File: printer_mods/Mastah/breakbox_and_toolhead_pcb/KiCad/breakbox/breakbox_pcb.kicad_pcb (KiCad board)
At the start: 2 copper layers, 60 x 50 mm, 18 parts

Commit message: Update PCBs and fix some issues
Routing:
- net (no net): track 621.3 -> 626.9 mm
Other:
- board text added: "V1.1 Breakbox Design by Mastah"
- board text removed: "V1.0 Breakbox Design by Mastah"
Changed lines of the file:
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@@
     (effects (font (size 0.6 0.6) (thickness 0.1)))
   )
-  (gr_text "V1.0\n\nBreakbox\n\nDesign by\nMastah" (at 87.3 79) (layer "F.SilkS")
+  (gr_text "V1.1\n\nBreakbox\n\nDesign by\nMastah" (at 87.3 79) (layer "F.SilkS")
     (effects (font (size 0.6 0.6) (thickness 0.1)) (justify left))
   )
@@
     (effects (font (size 0.6 0.6) (thickness 0.1)))
   )
-  (gr_text "Fan0\nVCC" (at 70.7 76.2) (layer "F.SilkS")
+  (gr_text "Fan0\nVCC" (at 73.5 76.2) (layer "F.SilkS")
     (effects (font (size 0.6 0.6) (thickness 0.1)))
   )
@@
     (effects (font (size 0.6 0.6) (thickness 0.1)))
   )
-  (gr_text "Fan0\nGND" (at 73.5 76.2) (layer "F.SilkS")
+  (gr_text "Fan0\nGND" (at 70.8 76.2) (layer "F.SilkS")
     (effects (font (size 0.6 0.6) (thickness 0.1)))
   )
@@
     (effects (font (size 0.6 0.6) (thickness 0.1)))
   )
-  (gr_text "Fan1\nGND" (at 82.3 76.2) (layer "F.SilkS")
+  (gr_text "Fan1\nGND" (at 79.5 76.2) (layer "F.SilkS")
     (effects (font (size 0.6 0.6) (thickness 0.1)))
   )
@@
     (effects (font (size 0.6 0.6) (thickness 0.1)))
   )
-  (gr_text "Fan1\nVCC" (at 79.6 76.2) (layer "F.SilkS")
+  (gr_text "Fan1\nVCC" (at 82.3 76.2) (layer "F.SilkS")
     (effects (font (size 0.6 0.6) (thickness 0.1)))
   )
@@
   (segment (start 73.3 83.125) (end 73.3 81.525) (width 0.508) (layer "F.Cu") (net 0))
   (segment (start 90 63) (end 97 63) (width 1.524) (layer "F.Cu") (net 0))
-  (segment (start 70.85 72.3) (end 70.85 70.85) (width 0.762) (layer "F.Cu") (net 0))
   (segment (start 76.6 58) (end 99.4 58) (width 0.762) (layer "F.Cu") (net 0))
   (segment (start 78.37 59.97) (end 83.4 65) (width 0.508) (layer "F.Cu") (net 0))
+  (segment (start 73.35 72.3) (end 73.35 70.65) (width 0.762) (layer "F.Cu") (net 0))
   (segment (start 87.2 95.8) (end 92.7 95.8) (width 0.762) (layer "F.Cu") (net 0))
   (segment (start 88.5 59.97) (end 88.5 61.5) (width 1.524) (layer "F.Cu") (net 0))
   (segment (start 59.3 73.9) (end 60.7 75.3) (width 0.508) (layer "F.Cu") (net 0))
-  (segment (start 79.65 72.3) (end 79.65 70.45) (width 0.762) (layer "F.Cu") (net 0))
   (segment (start 81.4 93.8) (end 81.4 92.5) (width 0.762) (layer "F.Cu") (net 0))
   (segment (start 92.7 85.4) (end 94.1 84) (width 0.762) (layer "F.Cu") (net 0))
+  (segment (start 73.35 70.65) (end 75 69) (width 0.762) (layer "F.Cu") (net 0))
   (segment (start 62.7 59.1) (end 63.8 58) (width 0.762) (layer "F.Cu") (net 0))
-  (segment (start 72.7 69) (end 81.8 69) (width 0.762) (layer "F.Cu") (net 0))
   (segment (start 68.2 90.95) (end 70.55 88.6) (width 0.508) (layer "F.Cu") (net 0))
   (segment (start 95.1 87) (end 97 87) (width 0.762) (layer "F.Cu") (net 0))
+  (segment (start 83.7 69) (end 88.3 69) (width 0.762) (layer "F.Cu") (net 0))
   (segment (start 97 68.6) (end 97 69) (width 0.508) (layer "F.Cu") (net 0))
   (segment (start 83.4 65) (end 96 65) (width 0.508) (layer "F.Cu") (net 0))
@@
   (segment (start 86.4 93.8) (end 86.4 95) (width 0.762) (layer "F.Cu") (net 0))
   (segment (start 92.7 95.8) (end 100 88.5) (width 0.762) (layer "F.Cu") (net 0))
-  (segment (start 81.8 69) (end 94 69) (width 0.762) (layer "F.Cu") (net 0))
   (segment (start 94.1 84) (end 97 84) (width 0.762) (layer "F.Cu") (net 0))
   (segment (start 98.5 73.5) (end 100 75) (width 0.508) (layer "F.Cu") (net 0))
@@
   (segment (start 93.5 82.5) (end 98.5 82.5) (width 0.508) (layer "F.Cu") (net 0))
   (segment (start 83.6 90.3) (end 90.8 90.3) (width 0.762) (layer "F.Cu") (net 0))
-  (segment (start 79.65 70.45) (end 81.1 69) (width 0.762) (layer "F.Cu") (net 0))
-  (segment (start 70.85 70.85) (end 72.7 69) (width 0.762) (layer "F.Cu") (net 0))
   (segment (start 87.4 88.6) (end 93.5 82.5) (width 0.508) (layer "F.Cu") (net 0))
-  (segment (start 94 69) (end 97 72) (width 0.762) (layer "F.Cu") (net 0))
   (segment (start 83.9 92.2) (end 84.4 91.7) (width 0.762) (layer "F.Cu") (net 0))
   (segment (start 63.8 58) (end 76.6 58) (width 0.762) (layer "F.Cu") (net 0))
@@
   (segment (start 92.9 81) (end 97 81) (width 0.508) (layer "F.Cu") (net 0))
   (segment (start 56.8 74.1) (end 59.1 76.4) (width 0.508) (layer "F.Cu") (net 0))
+  (segment (start 82.15 70.55) (end 83.7 69) (width 0.762) (layer "F.Cu") (net 0))
+  (segment (start 82.15 72.3) (end 82.15 70.55) (width 0.762) (layer "F.Cu") (net 0))
   (segment (start 69.8 62.2) (end 78.4 62.2) (width 0.508) (layer "F.Cu") (net 0))
   (segment (start 71.15 79.8) (end 80.9 79.8) (width 0.508) (layer "F.Cu") (net 0))
@@
   (segment (start 94.2 88.9) (end 94.2 87.9) (width 0.762) (layer "F.Cu") (net 0))
   (segment (start 58.1 79.8) (end 55.5 82.4) (width 0.508) (layer "F.Cu") (net 0))
-  (segment (start 81.1 69) (end 81.8 69) (width 0.762) (layer "F.Cu") (net 0))
   (segment (start 68.2 93.8) (end 68.2 90.95) (width 0.508) (layer "F.Cu") (net 0))
   (segment (start 65.7 93.8) (end 65.7 90.9) (width 0.508) (layer "F.Cu") (net 0))
   (segment (start 82.1 81) (end 82.1 83.15) (width 0.508) (layer "F.Cu") (net 0))
+  (segment (start 94 69) (end 97 72) (width 0.762) (layer "F.Cu") (net 0))
+  (segment (start 75 69) (end 94 69) (width 0.762) (layer "F.Cu") (net 0))
   (segment (start 70.8 83.125) (end 70.8 81.7) (width 0.508) (layer "F.Cu") (net 0))
   (segment (start 58 82.2) (end 58 83.225) (width 0.508) (layer "F.Cu") (net 0))
@@
   (segment (start 75.4 58) (end 76.6 58) (width 0.508) (layer "F.Cu") (net 0))
   (segment (start 95.4 79.5) (end 98.5 79.5) (width 0.508) (layer "B.Cu") (net 0))
-  (segment (start 82.15 72.7) (end 82.15 71.35) (width 0.508) (layer "B.Cu") (net 0))
   (segment (start 97.5 93.8) (end 102 89.3) (width 0.762) (layer "B.Cu") (net 0))
+  (segment (start 80.3 70.5) (end 98.5 70.5) (width 0.508) (layer "B.Cu") (net 0))
   (segment (start 98.5 79.5) (end 100 78) (width 0.508) (layer "B.Cu") (net 0))
   (segment (start 62.5 74.5) (end 91.2 74.5) (width 0.508) (layer "B.Cu") (net 0))
+  (segment (start 70.85 72.3) (end 70.85 70.75) (width 0.508) (layer "B.Cu") (net 0))
   (segment (start 94.2 60.4) (end 98.4 60.4) (width 1.524) (layer "B.Cu") (net 0))
-  (segment (start 82.15 71.35) (end 83 70.5) (width 0.508) (layer "B.Cu") (net 0))
+  (segment (start 98.5 70.5) (end 100 72) (width 0.508) (layer "B.Cu") (net 0))
   (segment (start 61.8 73.8) (end 62.5 74.5) (width 0.508) (layer "B.Cu") (net 0))
   (segment (start 85.5 59.97) (end 85.5 61.3) (width 1.524) (layer "B.Cu") (net 0))
-  (segment (start 98.5 67.5) (end 100 69) (width 0.508) (layer "B.Cu") (net 0))
   (segment (start 102 89.3) (end 102 86) (width 0.762) (layer "B.Cu") (net 0))
   (segment (start 87 87.9) (end 95.4 79.5) (width 0.508) (layer "B.Cu") (net 0))
   (segment (start 102 86) (end 100 84) (width 0.762) (layer "B.Cu") (net 0))
+  (segment (start 74.1 67.5) (end 98.5 67.5) (width 0.508) (layer "B.Cu") (net 0))
   (segment (start 73.8 87.9) (end 87 87.9) (width 0.508) (layer "B.Cu") (net 0))
-  (segment (start 73.35 70.35) (end 76.2 67.5) (width 0.508) (layer "B.Cu") (net 0))
+  (segment (start 98.5 67.5) (end 100 69) (width 0.508) (layer "B.Cu") (net 0))
   (segment (start 87.2 63) (end 91.6 63) (width 1.524) (layer "B.Cu") (net 0))
   (segment (start 98.4 60.4) (end 100 62) (width 1.524) (layer "B.Cu") (net 0))
-  (segment (start 98.5 70.5) (end 100 72) (width 0.508) (layer "B.Cu") (net 0))
   (segment (start 70.7 93.8) (end 70.7 91) (width 0.508) (layer "B.Cu") (net 0))
   (segment (start 88.9 93.8) (end 97.5 93.8) (width 0.762) (layer "B.Cu") (net 0))
-  (segment (start 76.2 67.5) (end 98.5 67.5) (width 0.508) (layer "B.Cu") (net 0))
-  (segment (start 83 70.5) (end 98.5 70.5) (width 0.508) (layer "B.Cu") (net 0))
+  (segment (start 70.85 70.75) (end 74.1 67.5) (width 0.508) (layer "B.Cu") (net 0))
+  (segment (start 79.65 72.3) (end 79.65 71.15) (width 0.508) (layer "B.Cu") (net 0))
   (segment (start 85.5 61.3) (end 87.2 63) (width 1.524) (layer "B.Cu") (net 0))
   (segment (start 91.6 63) (end 94.2 60.4) (width 1.524) (layer "B.Cu") (net 0))
   (segment (start 100 62) (end 100 63) (width 1.524) (layer "B.Cu") (net 0))
   (segment (start 91.2 74.5) (end 94.7 78) (width 0.508) (layer "B.Cu") (net 0))
+  (segment (start 79.65 71.15) (end 80.3 70.5) (width 0.508) (layer "B.Cu") (net 0))
   (segment (start 70.7 91) (end 73.8 87.9) (width 0.508) (layer "B.Cu") (net 0))
   (segment (start 94.7 78) (end 97 78) (width 0.508) (layer "B.Cu") (net 0))
   (segment (start 61.8 72.325) (end 61.8 73.8) (width 0.508) (layer "B.Cu") (net 0))
-  (segment (start 73.35 72.7) (end 73.35 70.35) (width 0.508) (layer "B.Cu") (net 0))
 )

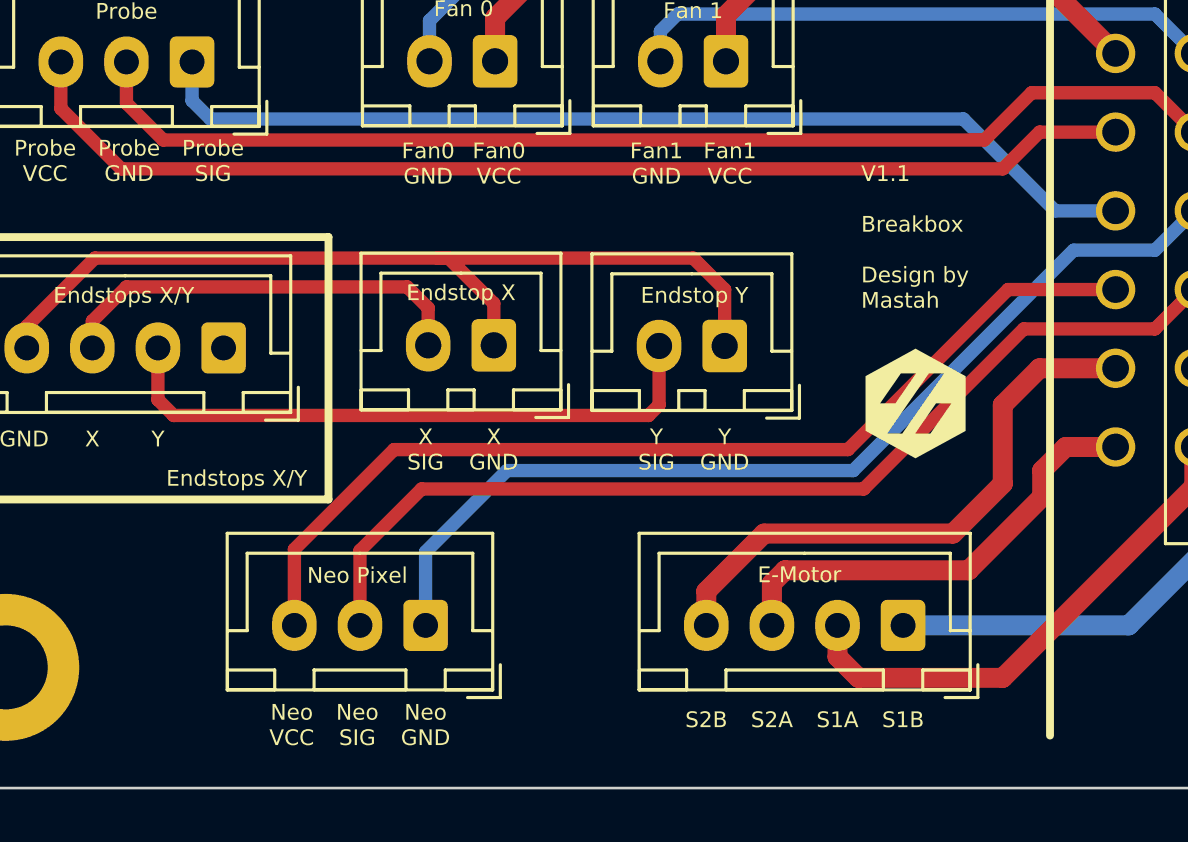
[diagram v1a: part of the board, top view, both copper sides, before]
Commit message: Update breakbox to add a filter for neopixel data (corruption over a long distance)
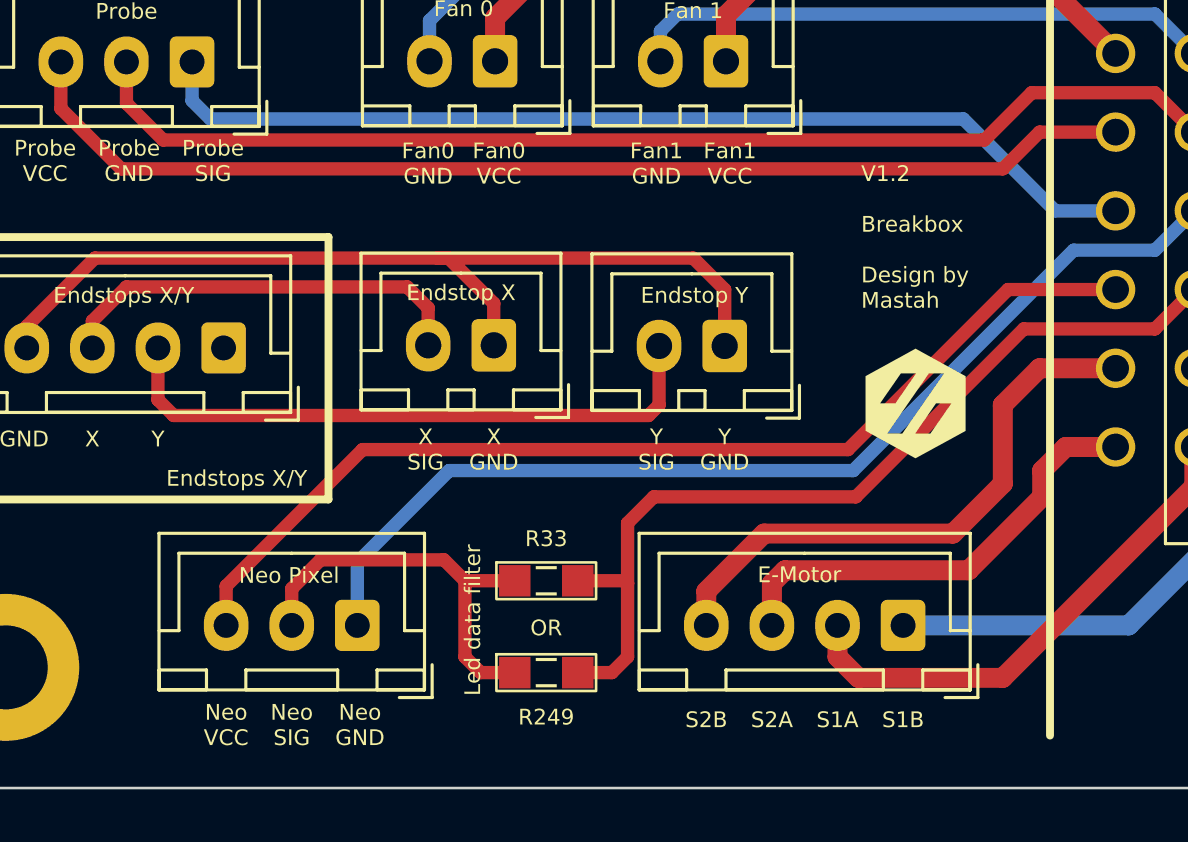
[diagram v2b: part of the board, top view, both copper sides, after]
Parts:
- added REF**: CR0805-FX-1101ELF, voron_resistor:CR0805-FX-1101ELF, F.Cu at (75.3, 95.6)
- added REF**: CR0805-FX-1101ELF, voron_resistor:CR0805-FX-1101ELF, F.Cu at (75.3, 92.1)
- moved Neo Pixel 2.60 mm to (68.1, 93.8)
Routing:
- net (no net): track 626.9 -> 642.5 mm
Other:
- board text added: "Led data filter"
- board text added: "OR"
- board text added: "R249"
- board text added: "R33"
- board text added: "V1.2 Breakbox Design by Mastah"
- board text removed: "V1.1 Breakbox Design by Mastah"
